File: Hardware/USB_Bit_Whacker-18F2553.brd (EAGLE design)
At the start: 25.4 x 40.6 mm, 23 parts, among them Q1 24MHz, U2 PIC18F2455, X1 USBSMD

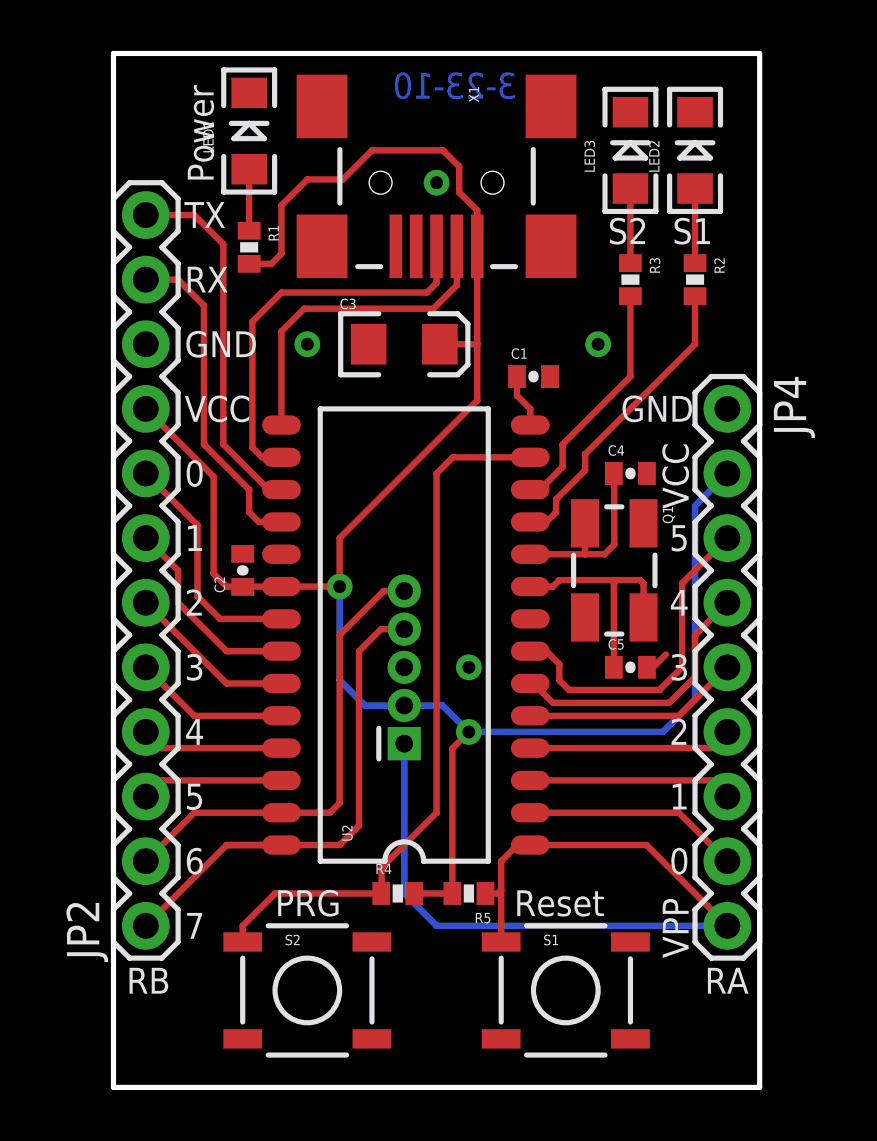
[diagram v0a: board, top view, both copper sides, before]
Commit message: added board fiducials
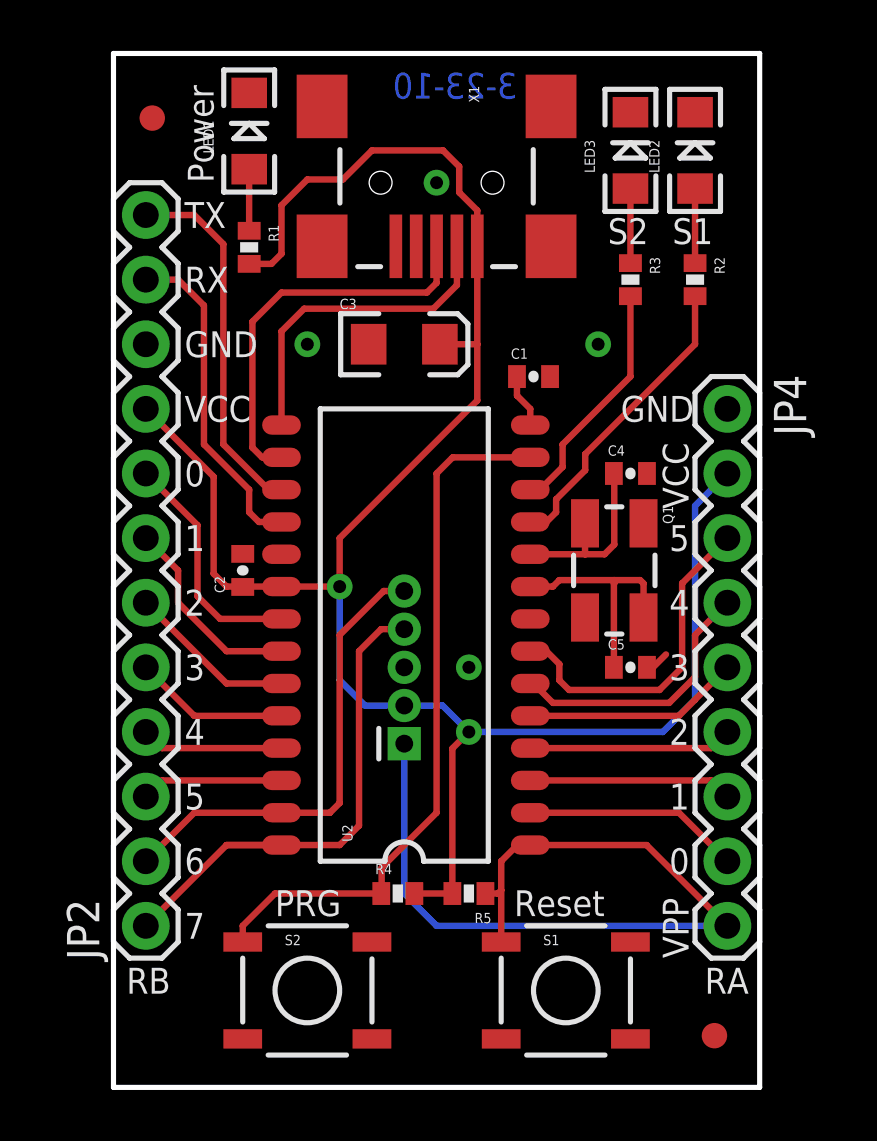
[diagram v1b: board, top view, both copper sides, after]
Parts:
- added FID1, FID2: FIDUCIAL1X2, SparkFun-Aesthetics:FIDUCIAL-1X2
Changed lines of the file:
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@@
 <?xml version="1.0" encoding="utf-8"?>
 <!DOCTYPE eagle SYSTEM "eagle.dtd">
-<eagle version="7.2.0">
+<eagle version="7.5.0">
 <drawing>
 <settings>
@@
 <setting verticaltext="up"/>
 </settings>
-<grid distance="0.05" unitdist="inch" unit="inch" style="lines" multiple="1" display="yes" altdistance="0.005" altunitdist="inch" altunit="inch"/>
+<grid distance="0.01" unitdist="inch" unit="inch" style="lines" multiple="1" display="yes" altdistance="0.001" altunitdist="inch" altunit="inch"/>
 <layers>
 <layer number="1" name="Top" color="4" fill="1" visible="yes" active="yes"/>
@@
 <layer number="18" name="Vias" color="2" fill="1" visible="yes" active="yes"/>
 <layer number="19" name="Unrouted" color="6" fill="1" visible="yes" active="yes"/>
-<layer number="20" name="Dimension" color="15" fill="1" visible="yes" active="yes"/>
-<layer number="21" name="tPlace" color="16" fill="1" visible="yes" active="yes"/>
-<layer number="22" name="bPlace" color="14" fill="1" visible="yes" active="yes"/>
+<layer number="20" name="Dimension" color="6" fill="1" visible="yes" active="yes"/>
+<layer number="21" name="tPlace" color="6" fill="1" visible="yes" active="yes"/>
+<layer number="22" name="bPlace" color="6" fill="1" visible="yes" active="yes"/>
 <layer number="23" name="tOrigins" color="15" fill="1" visible="yes" active="yes"/>
 <layer number="24" name="bOrigins" color="15" fill="1" visible="yes" active="yes"/>
@@
 <layer number="54" name="bGND_GNDA" color="1" fill="9" visible="no" active="no"/>
 <layer number="56" name="wert" color="7" fill="1" visible="no" active="yes"/>
+<layer number="57" name="tCAD" color="7" fill="1" visible="no" active="no"/>
+<layer number="59" name="tCarbon" color="7" fill="1" visible="no" active="no"/>
+<layer number="60" name="bCarbon" color="7" fill="1" visible="no" active="no"/>
+<layer number="90" name="Modules" color="5" fill="1" visible="no" active="no"/>
 <layer number="91" name="Nets" color="2" fill="1" visible="no" active="no"/>
 <layer number="92" name="Busses" color="1" fill="1" visible="no" active="no"/>
@@
 <layer number="97" name="Info" color="7" fill="1" visible="no" active="no"/>
 <layer number="98" name="Guide" color="6" fill="1" visible="no" active="no"/>
+<layer number="99" name="SpiceOrder" color="7" fill="1" visible="no" active="no"/>
 <layer number="100" name="Muster" color="7" fill="1" visible="no" active="no"/>
 <layer number="101" name="Patch_Top" color="12" fill="4" visible="no" active="yes"/>
@@
 <layer number="106" name="bPlate" color="7" fill="1" visible="no" active="yes"/>
 <layer number="107" name="Crop" color="7" fill="1" visible="no" active="yes"/>
+<layer number="108" name="tplace-old" color="10" fill="1" visible="yes" active="yes"/>
+<layer number="109" name="ref-old" color="11" fill="1" visible="yes" active="yes"/>
+<layer number="110" name="fp0" color="7" fill="1" visible="yes" active="yes"/>
+<layer number="111" name="LPC17xx" color="7" fill="1" visible="yes" active="yes"/>
+<layer number="112" name="tSilk" color="7" fill="1" visible="yes" active="yes"/>
+<layer number="113" name="IDFDebug" color="4" fill="1" visible="yes" active="yes"/>
 <layer number="116" name="Patch_BOT" color="9" fill="4" visible="no" active="yes"/>
 <layer number="121" name="_tsilk" color="7" fill="1" visible="no" active="yes"/>
 <layer number="122" name="_bsilk" color="7" fill="1" visible="no" active="yes"/>
+<layer number="123" name="tTestmark" color="7" fill="1" visible="yes" active="yes"/>
+<layer number="124" name="bTestmark" color="7" fill="1" visible="yes" active="yes"/>
+<layer number="125" name="_tNames" color="7" fill="1" visible="yes" active="yes"/>
+<layer number="126" name="_bNames" color="7" fill="1" visible="yes" active="yes"/>
+<layer number="127" name="_tValues" color="7" fill="1" visible="yes" active="yes"/>
+<layer number="128" name="_bValues" color="7" fill="1" visible="yes" active="yes"/>
+<layer number="129" name="Mask" color="7" fill="1" visible="yes" active="yes"/>
+<layer number="131" name="tAdjust" color="7" fill="1" visible="yes" active="yes"/>
+<layer number="132" name="bAdjust" color="7" fill="1" visible="yes" active="yes"/>
+<layer number="144" name="Drill_legend" color="7" fill="1" visible="yes" active="yes"/>
+<layer number="150" name="Notes" color="7" fill="1" visible="yes" active="yes"/>
 <layer number="151" name="HeatSink" color="7" fill="1" visible="no" active="yes"/>
+<layer number="152" name="_bDocu" color="7" fill="1" visible="yes" active="yes"/>
+<layer number="153" name="FabDoc1" color="7" fill="1" visible="yes" active="yes"/>
+<layer number="154" name="FabDoc2" color="7" fill="1" visible="yes" active="yes"/>
+<layer number="155" name="FabDoc3" color="7" fill="1" visible="yes" active="yes"/>
+<layer number="199" name="Contour" color="7" fill="1" visible="yes" active="yes"/>
 <layer number="200" name="200bmp" color="1" fill="10" visible="no" active="no"/>
 <layer number="201" name="201bmp" color="2" fill="1" visible="no" active="no"/>
@@
 <layer number="207" name="207bmp" color="8" fill="10" visible="no" active="yes"/>
 <layer number="208" name="208bmp" color="9" fill="10" visible="no" active="yes"/>
+<layer number="209" name="209bmp" color="7" fill="1" visible="yes" active="yes"/>
+<layer number="210" name="210bmp" color="7" fill="1" visible="yes" active="yes"/>
+<layer number="211" name="211bmp" color="7" fill="1" visible="yes" active="yes"/>
+<layer number="212" name="212bmp" color="7" fill="1" visible="yes" active="yes"/>
+<layer number="213" name="213bmp" color="7" fill="1" visible="yes" active="yes"/>
+<layer number="214" name="214bmp" color="7" fill="1" visible="yes" active="yes"/>
+<layer number="215" name="215bmp" color="7" fill="1" visible="yes" active="yes"/>
+<layer number="216" name="216bmp" color="7" fill="1" visible="yes" active="yes"/>
+<layer number="217" name="217bmp" color="18" fill="1" visible="no" active="no"/>
+<layer number="218" name="218bmp" color="19" fill="1" visible="no" active="no"/>
+<layer number="219" name="219bmp" color="20" fill="1" visible="no" active="no"/>
+<layer number="220" name="220bmp" color="21" fill="1" visible="no" active="no"/>
+<layer number="221" name="221bmp" color="22" fill="1" visible="no" active="no"/>
+<layer number="222" name="222bmp" color="23" fill="1" visible="no" active="no"/>
+<layer number="223" name="223bmp" color="24" fill="1" visible="no" active="no"/>
+<layer number="224" name="224bmp" color="25" fill="1" visible="no" active="no"/>
+<layer number="225" name="225bmp" color="7" fill="1" visible="yes" active="yes"/>
+<layer number="226" name="226bmp" color="7" fill="1" visible="yes" active="yes"/>
+<layer number="227" name="227bmp" color="7" fill="1" visible="yes" active="yes"/>
+<layer number="228" name="228bmp" color="7" fill="1" visible="yes" active="yes"/>
+<layer number="229" name="229bmp" color="7" fill="1" visible="yes" active="yes"/>
+<layer number="230" name="230bmp" color="7" fill="1" visible="yes" active="yes"/>
+<layer number="231" name="231bmp" color="7" fill="1" visible="yes" active="yes"/>
+<layer number="248" name="Housing" color="7" fill="1" visible="yes" active="yes"/>
+<layer number="249" name="Edge" color="7" fill="1" visible="yes" active="yes"/>
 <layer number="250" name="Descript" color="3" fill="1" visible="no" active="no"/>
 <layer number="251" name="SMDround" color="12" fill="11" visible="no" active="no"/>
 <layer number="254" name="cooling" color="7" fill="1" visible="no" active="yes"/>
+<layer number="255" name="routoute" color="7" fill="1" visible="yes" active="yes"/>
 </layers>
 <board>
@@
 <element name="JP4" library="SparkFun" package="1X09" value="" x="24.13" y="26.67" rot="R270"/>
 <element name="U$2" library="SparkFun" package="CREATIVE_COMMONS" value="CREATIVE_COMMONS" x="19.05" y="-7.62"/>
+<element name="FID1" library="SparkFun-Aesthetics" package="FIDUCIAL-1X2" value="FIDUCIAL1X2" x="1.524" y="38.1"/>
+<element name="FID2" library="SparkFun-Aesthetics" package="FIDUCIAL-1X2" value="FIDUCIAL1X2" x="23.622" y="2.032"/>
 </elements>
 <signals>
